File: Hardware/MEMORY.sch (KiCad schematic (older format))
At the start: 9 parts, among them J8 Micro_SD_Card, U5 M24C64-WDW6TP

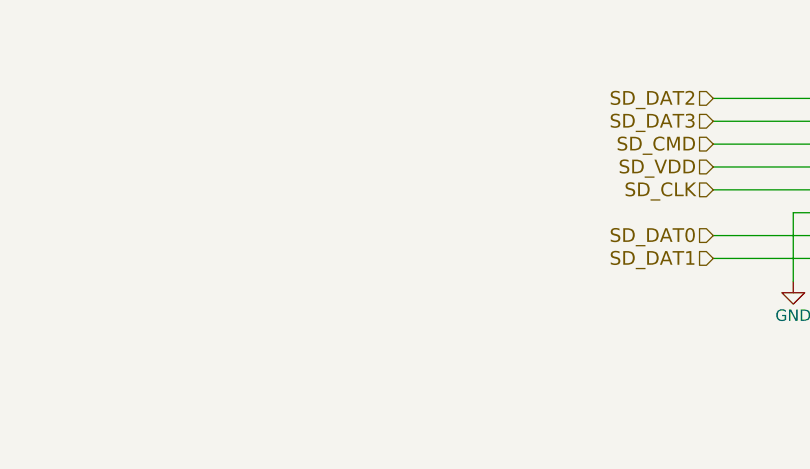
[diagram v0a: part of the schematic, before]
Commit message: Added additional headers to some interfaces, GPIOs, and FTDI pins. Added silks
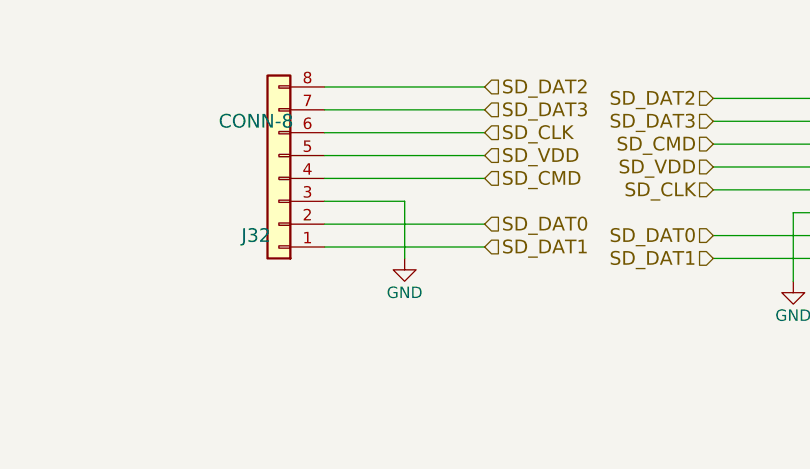
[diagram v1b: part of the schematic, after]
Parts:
- added J32: CONN-8, Connector_PinHeader_2.54mm:PinHeader_1x08_P2.54mm_Vertical, symbol Connector_Generic:Conn_01x08
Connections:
- net GND: now also J32.3 (Pin_3)
- net SD_CLK: now also J32.6 (Pin_6)
- net SD_CMD: now also J32.4 (Pin_4)
- net SD_DAT0: now also J32.2 (Pin_2)
- net SD_DAT1: now also J32.1 (Pin_1)
- net SD_DAT2: now also J32.8 (Pin_8)
- net SD_DAT3: now also J32.7 (Pin_7)
- net SD_VDD: now also J32.5 (Pin_5)
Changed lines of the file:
@@
 $Descr A4 11693 8268
 encoding utf-8
-Sheet 4 10
+Sheet 3 10
 Title ""
 Date ""
@@
 Text HLabel 6950 1800 0    60   Input ~ 0
 SD_CMD
-Text HLabel 6950 2200 0    60   Input ~ 0
-SD_DAT0
 Text HLabel 6950 2000 0    60   Input ~ 0
 SD_CLK
@@
 Wire Wire Line
 	1900 4800 2150 4800
+$Comp
+L Connector_Generic:Conn_01x08 J?
+U 1 1 6029DDFA
+P 5050 1950
+AR Path="/59234D3B/6029DDFA" Ref="J?"  Part="1"
+AR Path="/5920635A/6029DDFA" Ref="J32"  Part="1"
+F 0 "J32" H 5150 2200 60  0000 C CNN
+F 1 "CONN-8" H 5150 1700 60  0000 C CNN
+F 2 "Connector_PinHeader_2.54mm:PinHeader_1x08_P2.54mm_Vertical" H 5050 2000 60  0001 C CNN
+F 3 "http://www.jst-mfg.com/product/pdf/eng/eGH.pdf" H 5050 2000 60  0001 C CNN
+F 4 "CONN-008" H 5250 2300 60  0001 C CNN "part_num"
+	1    5050 1950
+	-1   0    0    1
+$EndComp
+Wire Wire Line
+	5250 1550 5950 1550
+Wire Wire Line
+	5950 2250 5250 2250
+Wire Wire Line
+	5250 2150 5950 2150
+Wire Wire Line
+	5250 1950 5950 1950
+Wire Wire Line
+	5250 1850 5950 1850
+Wire Wire Line
+	5250 1750 5950 1750
+Wire Wire Line
+	5250 1650 5950 1650
+Text HLabel 5950 1550 2    60   Input ~ 0
+SD_DAT2
+Text HLabel 5950 1650 2    60   Input ~ 0
+SD_DAT3
+Text HLabel 5950 1950 2    60   Input ~ 0
+SD_CMD
+Text HLabel 5950 1850 2    60   Input ~ 0
+SD_VDD
+Text HLabel 5950 1750 2    60   Input ~ 0
+SD_CLK
+Text HLabel 6950 2200 0    60   Input ~ 0
+SD_DAT0
+Text HLabel 5950 2150 2    60   Input ~ 0
+SD_DAT0
+Text HLabel 5950 2250 2    60   Input ~ 0
+SD_DAT1
+$Comp
+L power:GND #PWR0112
+U 1 1 602A5B61
+P 5600 2300
+F 0 "#PWR0112" H 5600 2050 50  0001 C CNN
+F 1 "GND" H 5600 2150 50  0000 C CNN
+F 2 "" H 5600 2300 50  0001 C CNN
+F 3 "" H 5600 2300 50  0001 C CNN
+	1    5600 2300
+	1    0    0    -1
+$EndComp
+Wire Wire Line
+	5600 2300 5600 2050
+Wire Wire Line
+	5250 2050 5600 2050
 $EndSCHEMATC

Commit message: associated components to their JLC part numbers
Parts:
- R21, R23, R25: LCSC (none) -> C21189
- R22, R24, R26, R27: LCSC (none) -> C25804
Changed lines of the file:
@@
 EESchema Schematic File Version 4
-LIBS:ZP-Breakout-cache
-EELAYER 29 0
+EELAYER 30 0
 EELAYER END
 $Descr A4 11693 8268
@@
 F 3 "http://industrial.panasonic.com/www-cgi/jvcr13pz.cgi?E+PZ+3+AOA0001+ERJ3GEYJ103V+7+WW" H 1650 5650 50  0001 C CNN
 F 4 "RESS-005" V 1650 5650 60  0001 C CNN "part_num"
+F 5 "C25804" V 1650 5650 50  0001 C CNN "LCSC"
 	1    1650 5650
 	1    0    0    -1
@@
 F 3 "http://www.yageo.com/documents/recent/PYu-RC_Group_51_RoHS_L_10.pdf" H 1650 5100 50  0001 C CNN
 F 4 "RESS-001" V 1650 5100 60  0001 C CNN "part_num"
+F 5 "C21189" V 1650 5100 50  0001 C CNN "LCSC"
 	1    1650 5100
 	1    0    0    -1
@@
 F 3 "http://industrial.panasonic.com/www-cgi/jvcr13pz.cgi?E+PZ+3+AOA0001+ERJ3GEYJ103V+7+WW" H 1900 5650 50  0001 C CNN
 F 4 "RESS-005" V 1900 5650 60  0001 C CNN "part_num"
+F 5 "C25804" V 1900 5650 50  0001 C CNN "LCSC"
 	1    1900 5650
 	1    0    0    -1
@@
 F 3 "http://industrial.panasonic.com/www-cgi/jvcr13pz.cgi?E+PZ+3+AOA0001+ERJ3GEYJ103V+7+WW" H 2150 5650 50  0001 C CNN
 F 4 "RESS-005" V 2150 5650 60  0001 C CNN "part_num"
+F 5 "C25804" V 2150 5650 50  0001 C CNN "LCSC"
 	1    2150 5650
 	1    0    0    -1
@@
 F 3 "http://www.yageo.com/documents/recent/PYu-RC_Group_51_RoHS_L_10.pdf" H 1900 5100 50  0001 C CNN
 F 4 "RESS-001" V 1900 5100 60  0001 C CNN "part_num"
+F 5 "C21189" V 1900 5100 50  0001 C CNN "LCSC"
 	1    1900 5100
 	1    0    0    -1
@@
 F 3 "http://www.yageo.com/documents/recent/PYu-RC_Group_51_RoHS_L_10.pdf" H 2150 5100 50  0001 C CNN
 F 4 "RESS-001" V 2150 5100 60  0001 C CNN "part_num"
+F 5 "C21189" V 2150 5100 50  0001 C CNN "LCSC"
 	1    2150 5100
 	1    0    0    -1
@@
 F 3 "http://industrial.panasonic.com/www-cgi/jvcr13pz.cgi?E+PZ+3+AOA0001+ERJ3GEYJ103V+7+WW" H 3950 5300 50  0001 C CNN
 F 4 "RESS-005" V 3950 5300 60  0001 C CNN "part_num"
+F 5 " C25804" V 3950 5300 50  0001 C CNN "LCSC"
 	1    3950 5300
 	1    0    0    -1
